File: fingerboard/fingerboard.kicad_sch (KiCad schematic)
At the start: 5 parts, among them J1 Conn_01x05_Pin, SW1 SW_Push, SW2 SW_Push, SW3 SW_Push, SW4 SW_Push

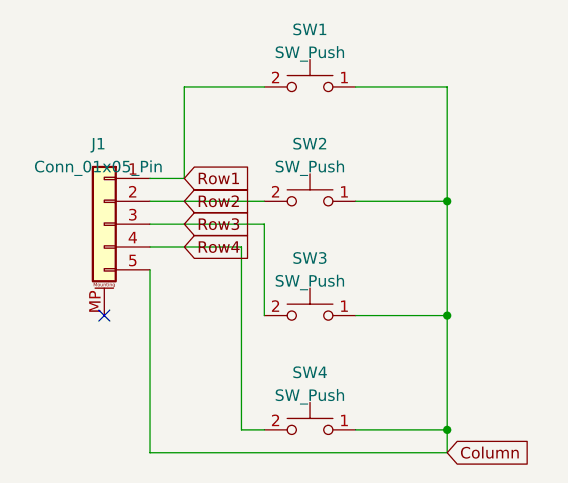
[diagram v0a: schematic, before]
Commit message: tweak fingerboard more, incl new pinout
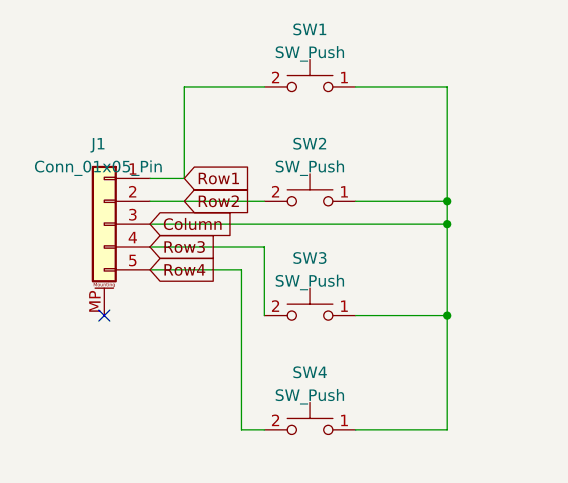
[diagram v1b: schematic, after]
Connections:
- net Column: now also J1.3 (Pin_3); no longer J1.5 (Pin_5)
- net Row3: now also J1.4 (Pin_4); no longer J1.3 (Pin_3)
- net Row4: now also J1.5 (Pin_5); no longer J1.4 (Pin_4)
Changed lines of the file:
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@@
   (junction (at 160.02 101.6) (diameter 0) (color 0 0 0 0)
   )
-  (junction (at 160.02 114.3) (diameter 0) (color 0 0 0 0)
+  (junction (at 160.02 91.44) (diameter 0) (color 0 0 0 0)
   )
   (junction (at 160.02 88.9) (diameter 0) (color 0 0 0 0)
@@
     (stroke (width 0) (type default))
   )
-  (wire (pts (xy 127 116.84) (xy 160.02 116.84))
-    (stroke (width 0) (type default))
-  )
-  (wire (pts (xy 139.7 91.44) (xy 139.7 101.6))
+  (wire (pts (xy 139.7 101.6) (xy 139.7 93.98))
     (stroke (width 0) (type default))
   )
@@
     (stroke (width 0) (type default))
   )
-  (wire (pts (xy 127 93.98) (xy 137.16 93.98))
-    (stroke (width 0) (type default))
-  )
-  (wire (pts (xy 127 96.52) (xy 127 116.84))
-    (stroke (width 0) (type default))
-  )
   (wire (pts (xy 130.81 76.2) (xy 139.7 76.2))
-    (stroke (width 0) (type default))
-  )
-  (wire (pts (xy 137.16 93.98) (xy 137.16 114.3))
     (stroke (width 0) (type default))
   )
@@
     (stroke (width 0) (type default))
   )
-  (wire (pts (xy 160.02 88.9) (xy 160.02 101.6))
+  (wire (pts (xy 160.02 88.9) (xy 160.02 91.44))
     (stroke (width 0) (type default))
   )
@@
     (stroke (width 0) (type default))
   )
+  (wire (pts (xy 137.16 114.3) (xy 137.16 96.52))
+    (stroke (width 0) (type default))
+  )
+  (wire (pts (xy 139.7 93.98) (xy 127 93.98))
+    (stroke (width 0) (type default))
+  )
   (wire (pts (xy 149.86 114.3) (xy 160.02 114.3))
+    (stroke (width 0) (type default))
+  )
+  (wire (pts (xy 137.16 96.52) (xy 127 96.52))
+    (stroke (width 0) (type default))
+  )
+  (wire (pts (xy 160.02 91.44) (xy 160.02 101.6))
     (stroke (width 0) (type default))
   )
@@
     (stroke (width 0) (type default))
   )
-  (wire (pts (xy 160.02 114.3) (xy 160.02 116.84))
+  (wire (pts (xy 149.86 76.2) (xy 160.02 76.2))
     (stroke (width 0) (type default))
   )
-  (wire (pts (xy 127 91.44) (xy 139.7 91.44))
-    (stroke (width 0) (type default))
-  )
-  (wire (pts (xy 149.86 76.2) (xy 160.02 76.2))
+  (wire (pts (xy 127 91.44) (xy 160.02 91.44))
     (stroke (width 0) (type default))
   )
@@
     )
   )
-  (global_label "Row4" (shape input) (at 130.81 93.98 0) (fields_autoplaced)
+  (global_label "Row4" (shape input) (at 127 96.52 0) (fields_autoplaced)
     (effects (font (size 1.27 1.27)) (justify left))
-    (property "Intersheetrefs" "${INTERSHEET_REFS}" (at 138.6748 93.98 0)
+    (property "Intersheetrefs" "${INTERSHEET_REFS}" (at 134.8648 96.52 0)
       (effects (font (size 1.27 1.27)) (justify left) hide)
     )
   )
-  (global_label "Column" (shape input) (at 160.02 116.84 0) (fields_autoplaced)
+  (global_label "Column" (shape input) (at 127 91.44 0) (fields_autoplaced)
     (effects (font (size 1.27 1.27)) (justify left))
-    (property "Intersheetrefs" "${INTERSHEET_REFS}" (at 170.0013 116.84 0)
+    (property "Intersheetrefs" "${INTERSHEET_REFS}" (at 136.9813 91.44 0)
       (effects (font (size 1.27 1.27)) (justify left) hide)
     )
   )
-  (global_label "Row3" (shape input) (at 130.81 91.44 0) (fields_autoplaced)
+  (global_label "Row3" (shape input) (at 127 93.98 0) (fields_autoplaced)
     (effects (font (size 1.27 1.27)) (justify left))
-    (property "Intersheetrefs" "${INTERSHEET_REFS}" (at 138.6748 91.44 0)
+    (property "Intersheetrefs" "${INTERSHEET_REFS}" (at 134.8648 93.98 0)
       (effects (font (size 1.27 1.27)) (justify left) hide)
     )
